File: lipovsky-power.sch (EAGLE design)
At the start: 95 parts, among them J1 M04-929J, J2 M04-929J, J3 M04-929J, J4 M04-929J, Q1 NMOS30V_30A, Q12 NMOS40V_10A, Q14 NMOS40V_10A, Q16 NMOS40V_10A, Q18 NMOS40V_10A, Q21 PMOS30V_11A, Q22 PMOS30V_11A, Q23 NMOS40V_10A, Q24 NMOS40V_10A, Q25 PMOS30V_11A, Q26 PMOS30V_11A, Q27 NMOS40V_10A, Q28 NMOS40V_10A, Q3 2PMOS50V_0.17A, Q31 PMOS30V_11A, Q32 PMOS30V_11A, Q33 PMOS30V_11A, Q34 PMOS30V_11A, Q35 PMOS30V_11A, Q36 PMOS30V_11A, Q37 PMOS30V_11A, Q38 PMOS30V_11A, Q4 2PMOS50V_0.17A, Q41 PMOS30V_11A, Q42 PMOS30V_11A, Q43 PMOS30V_11A, Q44 PMOS30V_11A, Q45 PMOS30V_11A, Q46 PMOS30V_11A, Q47 PMOS30V_11A, Q48 PMOS30V_11A, Q5 2NMOS30V_0.1A, Q51 PMOS30V_11A, Q52 PMOS30V_11A, Q53 PMOS30V_11A, Q54 PMOS30V_11A, Q55 PMOS30V_11A, Q56 PMOS30V_11A, Q57 PMOS30V_11A, Q58 PMOS30V_11A, Q62 PMOS30V_11A, Q64 PMOS30V_11A, Q66 PMOS30V_11A, Q68 PMOS30V_11A, T1 TFORM_4_4311_4A4, U1 DG508BEN-T1-GE4, U2 DG508BEN-T1-GE4, U4 LTC3805-5IDD, U6 AR30N60PPA-13

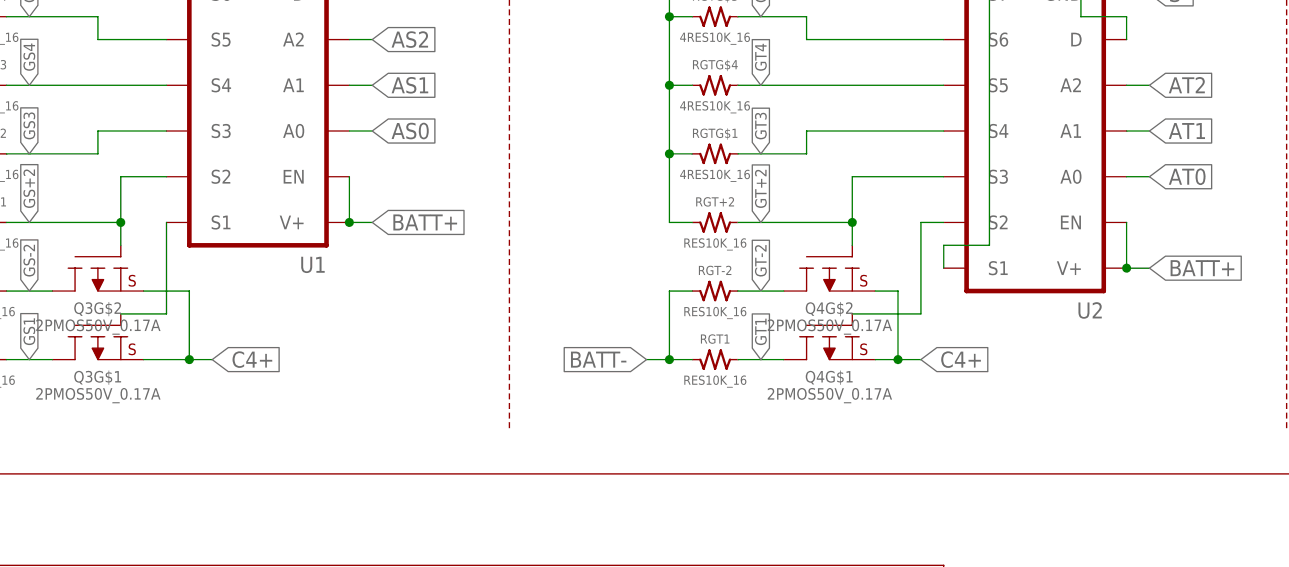
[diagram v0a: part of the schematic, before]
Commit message: Missed a couple pmos gate pull-ups
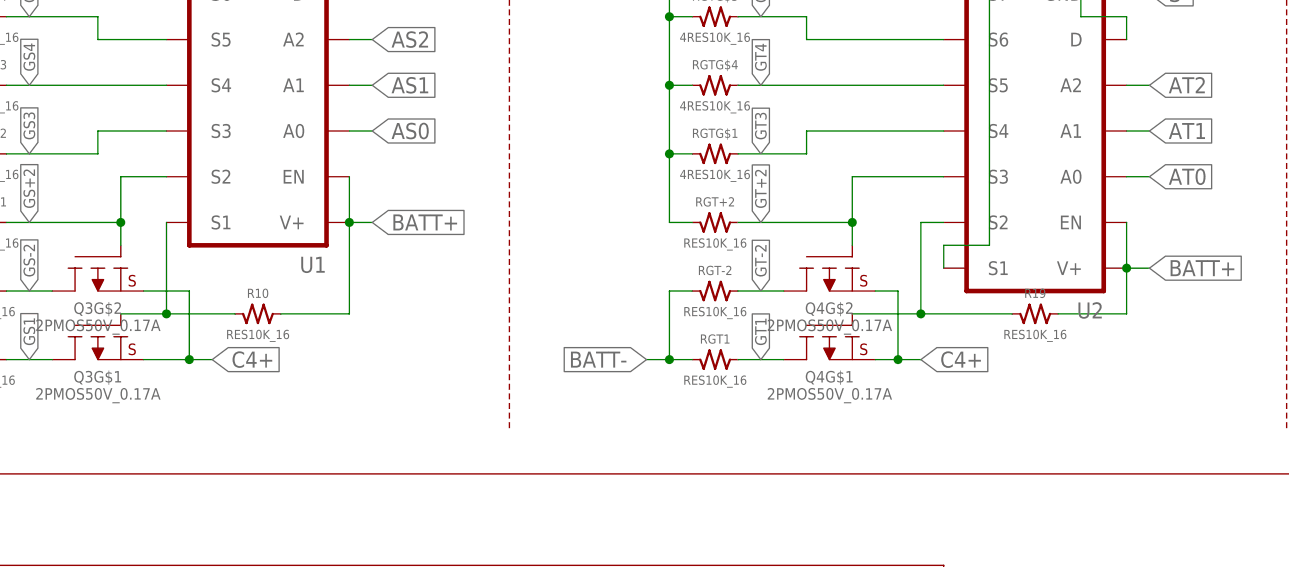
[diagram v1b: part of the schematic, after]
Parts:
- added R10, R19: RES10K_16, dubec:RES10K_16
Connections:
- net !GS1: now also R10.1
- net !GT1: now also R19.1
- net BATT+: now also R10.2, R19.2
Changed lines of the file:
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@@
 <part name="D1" library="dubec" deviceset="D_ZENER" device="18V_0.3W"/>
 <part name="R4" library="dubec" deviceset="RES" device="15.4K_16"/>
+<part name="R10" library="dubec" deviceset="RES" device="10K_16"/>
+<part name="R19" library="dubec" deviceset="RES" device="10K_16"/>
 </parts>
 <sheets>
@@
 <instance part="D1" gate="G$1" x="43.18" y="38.1" rot="R270"/>
 <instance part="R4" gate="G$1" x="27.94" y="38.1" rot="R90"/>
+<instance part="R10" gate="G$1" x="114.3" y="22.86"/>
+<instance part="R19" gate="G$1" x="200.66" y="22.86"/>
 </instances>
 <busses>
@@
 <wire x1="124.46" y1="38.1" x2="124.46" y2="33.02" width="0.1524" layer="91"/>
 <junction x="124.46" y="33.02"/>
+<wire x1="124.46" y1="33.02" x2="124.46" y2="22.86" width="0.1524" layer="91"/>
+<wire x1="124.46" y1="22.86" x2="116.84" y2="22.86" width="0.1524" layer="91"/>
+<pinref part="R10" gate="G$1" pin="2"/>
 </segment>
 <segment>
@@
 <wire x1="210.82" y1="33.02" x2="210.82" y2="27.94" width="0.1524" layer="91"/>
 <junction x="210.82" y="27.94"/>
+<pinref part="R19" gate="G$1" pin="2"/>
+<wire x1="203.2" y1="22.86" x2="210.82" y2="22.86" width="0.1524" layer="91"/>
+<wire x1="210.82" y1="22.86" x2="210.82" y2="27.94" width="0.1524" layer="91"/>
 </segment>
 </net>
@@
 <pinref part="U2" gate="G$1" pin="S2"/>
 <wire x1="190.5" y1="33.02" x2="187.96" y2="33.02" width="0.1524" layer="91"/>
+<pinref part="R19" gate="G$1" pin="1"/>
+<wire x1="187.96" y1="22.86" x2="198.12" y2="22.86" width="0.1524" layer="91"/>
+<junction x="187.96" y="22.86"/>
 </segment>
 </net>
@@
 <pinref part="Q3" gate="G$1" pin="G"/>
 <wire x1="104.14" y1="22.86" x2="99.06" y2="22.86" width="0.1524" layer="91"/>
-</segment>
-</net>
+<wire x1="104.14" y1="22.86" x2="111.76" y2="22.86" width="0.1524" layer="91"/>
+<junction x="104.14" y="22.86"/>
+<pinref part="R10" gate="G$1" pin="1"/>
+</segment>
+</net>

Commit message: test point
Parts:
- added TP4: TEST-POINT3, SparkFun-Passives:TEST-POINT3
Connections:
- net SS-5: now also TP4.1
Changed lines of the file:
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@@
 <part name="R10" library="dubec" deviceset="RES" device="10K_16"/>
 <part name="R19" library="dubec" deviceset="RES" device="10K_16"/>
+<part name="TP4" library="SparkFun-Passives" deviceset="TEST-POINT" device="3"/>
 </parts>
 <sheets>
@@
 <instance part="R10" gate="G$1" x="114.3" y="22.86"/>
 <instance part="R19" gate="G$1" x="200.66" y="22.86"/>
+<instance part="TP4" gate="G$1" x="-93.98" y="20.32" rot="R270"/>
 </instances>
 <busses>
@@
 <net name="SS+5" class="0">
 <segment>
-<wire x1="-96.52" y1="33.02" x2="-91.44" y2="33.02" width="0.1524" layer="91"/>
 <pinref part="Q51" gate="G$1" pin="S"/>
 <pinref part="Q52" gate="G$1" pin="S"/>
+<wire x1="-96.52" y1="33.02" x2="-91.44" y2="33.02" width="0.1524" layer="91"/>
 </segment>
 </net>
 <net name="SS-5" class="0">
 <segment>
-<wire x1="-91.44" y1="22.86" x2="-96.52" y2="22.86" width="0.1524" layer="91"/>
+<wire x1="-91.44" y1="22.86" x2="-93.98" y2="22.86" width="0.1524" layer="91"/>
 <pinref part="Q54" gate="G$1" pin="S"/>
 <pinref part="Q53" gate="G$1" pin="S"/>
-</segment>
-</net>
+<pinref part="TP4" gate="G$1" pin="1"/>
+<wire x1="-93.98" y1="22.86" x2="-96.52" y2="22.86" width="0.1524" layer="91"/>
+<wire x1="-93.98" y1="20.32" x2="-93.98" y2="22.86" width="0.1524" layer="91"/>
+<junction x="-93.98" y="22.86"/>
+</segment>
+</net>

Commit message: .
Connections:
- net FB: now also MVOE.PA7
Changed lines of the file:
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@@
 <wire x1="241.3" y1="-48.26" x2="241.3" y2="-45.72" width="0.1524" layer="91"/>
+</segment>
+<segment>
+<pinref part="MVOE" gate="G$1" pin="PA7"/>
+<wire x1="274.32" y1="48.26" x2="276.86" y2="48.26" width="0.1524" layer="91"/>
+<label x="276.86" y="48.26" size="1.27" layer="95" xref="yes"/>
 </segment>
 </net>

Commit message: 2S boost
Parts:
- removed D4: D_ZENER2.4V, dubec:D_ZENER2.4V
- removed MVOE: ATTINYX4A2MMHR, dubec:ATTINYX4A2MMHR
- added CB1, CB2, CB3: CAP4.7UF_10V, dubec:CAP4.7UF_10V
- added D2: D_ZENER2.4V, dubec:D_ZENER2.4V
- added DB1: 2D_SCHOTTKY40V_0.2A, dubec:2D_SCHOTTKY40V_0.2A
- added U3: DG508BEN-T1-GE4, dubec:DG508BEN-T1-GE4
- added U5: LM2665M6, dubec:LM2665M6
- U1: value DG508BEN-T1-GE4 -> LTC3805-5IDD; device dubec:DG508BEN-T1-GE4 -> dubec:LTC3805-5IDD
- U2: value DG508BEN-T1-GE4 -> ATTINYX4A2MMHR; device dubec:DG508BEN-T1-GE4 -> dubec:ATTINYX4A2MMHR
- U4: value LTC3805-5IDD -> DG508BEN-T1-GE4; device dubec:LTC3805-5IDD -> dubec:DG508BEN-T1-GE4
- renumbered U$2 to JP2, U$3 to DA1, U$4 to DA2
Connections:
- new net 2SBOOST: CB3.2, DB1G$1.A, DB1G$2.C, U5.OUT
- new net N$11: CB2.1, U5.CAP-
- new net N$2: CB1.2, DB1G$2.A, U5.V+
- new net N$9: CB2.2, U5.CAP+
- net !GS1: now also U3.S1; no longer U1.S1
- net !GT1: now also U4.S2; no longer U2.S2
- net !S_RESET: now also U2.PB3; no longer MVOE.PB3
- net +5V: now also U2.VCC; no longer MVOE.VCC
- net +8V: now also U1.VCC; no longer U4.VCC
- net AS0: now also U2.PA2, U3.A0; no longer MVOE.PA2, U1.A0
- net AS1: now also U2.PA1, U3.A1; no longer MVOE.PA1, U1.A1
- net AS2: now also U2.PA0, U3.A2; no longer MVOE.PA0, U1.A2
- net AT0: now also U2.PB2, U4.A0; no longer MVOE.PB2, U2.A0
- net AT1: now also U2.PB1, U4.A1; no longer MVOE.PB1, U2.A1
- net AT2: now also U2.PB0, U4.A2; no longer MVOE.PB0, U2.A2
- net BATT+: now also U3.EN, U3.V+, U4.EN, U4.V+; no longer U1.EN, U1.V+, U2.EN, U2.V+
- net BATT-: now also U3.D, U3.S7, U3.S8, U3.V-, U4.D, U4.S1, U4.S8, U4.V-; no longer U1.D, U1.S7, U1.S8, U1.V-, U2.D, U2.S1, U2.S8, U2.V-
- net C1: now also CB3.1, U5.GND, U5.SD
- net C2: now also CB1.1
- net C4+: now also DB1G$1.C
- net EN_FLYBACK: now also U1.RUN, U2.PA3; no longer MVOE.PA3, U4.RUN
- net FB: now also U2.PA7; no longer MVOE.PA7
- net GS+2: now also U3.S2; no longer U1.S2
- net GS3: now also U3.S3; no longer U1.S3
- net GS4: now also U3.S4; no longer U1.S4
- net GS5: now also U3.S5; no longer U1.S5
- net GS6: now also U3.S6; no longer U1.S6
- net GT+2: now also U4.S3; no longer U2.S3
- net GT3: now also U4.S4; no longer U2.S4
- net GT4: now also U4.S5; no longer U2.S5
- net GT5: now also U4.S6; no longer U2.S6
- net GT6: now also U4.S7; no longer U2.S7
- net MISO: now also U2.PA5; no longer MVOE.PA5
- net N$1: now also D2.C, U1.FB; no longer D4.C, U4.FB
- net N$12: now also U1.I_TH; no longer U4.I_TH
- net N$3: now also U1.FS; no longer U4.FS
- net N$4: now also U1.OC; no longer U4.OC
- net N$5: now also U1.GATE; no longer U4.GATE
- net N$6: now also U1.I_SENSE; no longer U4.I_SENSE
- net S-: now also D2.A, U1.SYNC, U3.GND; no longer D4.A, MVOE.GND, U4.SYNC
- net SCL: now also U2.PA4; no longer MVOE.PA4
- net SDA: now also U2.PA6; no longer MVOE.PA6
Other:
- note added: "2S Booster"
- moved on the sheet: J1, J2, J3, J4, JP1, Q12, Q14, Q16, Q18, Q21, Q22, Q23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

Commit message: Inductor routing
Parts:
- removed C9: CAP22P_50V, dubec:CAP22P_50V
- removed JP2: JUMPER-PAD, dubec:JUMPER-PAD
- removed Q5: 2NMOS30V_0.1A, dubec:2NMOS30V_0.1A
- removed R11: RES10K_16, dubec:RES10K_16
- removed R12: RES590_16, dubec:RES590_16
- removed R13: RES2.2K_16, dubec:RES2.2K_16
- removed R14: RES5.1K_16, dubec:RES5.1K_16
- removed R15: RES100K_16, dubec:RES100K_16
- removed T1: TFORM_4_4311_4A4, dubec:TFORM_4_4311_4A4
- removed TP2: TEST-POINT3, SparkFun-Passives:TEST-POINT3
- removed U6: AR30N60PPA-13, dubec:AR30N60PPA-13
- added L1: COUPINDSRF1260A3R3Y, dubec:COUPINDSRF1260A3R3Y
- C5: value CAP220U_6V3 -> CAP100UF_10V; device dubec:CAP220U_6V3 -> dubec:CAP100UF_10V
- D2: value D_ZENER2.4V -> D_SCH30V_5A; device dubec:D_ZENER2.4V -> dubec:D_SCH30V_5A
- R6: value RES61.9K_16 -> RES36K_16; device dubec:RES61.9K_16 -> dubec:RES36K_16
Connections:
- removed net N$1: D2.C, R11.1, U1.FB
- removed net N$18: C9.1, Q5G$1.D, R12.2
- removed net N$20: C9.2, R13.1
- removed net N$21: R13.2, U6.SYNC
- removed net N$24: R14.2, U6.TON
- removed net N$25: R15.2, U6.TOFF/EN
- removed net N$26: T1.1, U6.VD
- removed net N$8: T1.4, TP2.1
- removed net SFB: Q5G$2.G, U6.SFB
- net +8V: no longer R12.1
- net FB: no longer R11.2
- net N$10: now also L1.A2; no longer T1.5, T1.7
- net N$5: no longer Q5G$1.G
- net N$7: now also D2.A, L1.B2; no longer JP2.2, T1.3
- net OPTO_C: no longer Q5G$2.D
- net S+: now also L1.A1; no longer T1.6, T1.8
- net S-: now also U1.FB; no longer D2.A, Q5G$1.S
- net T+: now also D2.C; no longer T1.2, U6.VCC
- net T-: now also L1.B1; no longer JP2.1, Q5G$2.S, R14.1, R15.1, U6.GND, U6.VS
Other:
- moved on the sheet: C10, C5, R9

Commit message: "finished"
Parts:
- removed C4: CAP47N_25V, dubec:CAP47N_25V
- added D3: D_SCH30V_0.2A, dubec:D_SCH30V_0.2A
- R7: value RES2.2K_16 -> RES18.2K_16; device dubec:RES2.2K_16 -> dubec:RES18.2K_16
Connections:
- removed net N$12: R7.2, U1.I_TH
- removed net N$17: C4.2, R7.1
- new net N$1: D3.A, U1.I_TH
- new net TH: D3.C, R7.1
- net +8V: now also R7.2
- net S-: no longer C4.1
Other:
- moved on the sheet: C10, CB1, CB2, CB3, D2, DB1G$2, J1, J2, J3, J4, JP1, L1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

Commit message: Power board finished now
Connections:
- removed net TH: D3.C, R7.1
- net !S_RESET: now also J3.1; no longer J3.4
- net FB: now also D3.C, R7.1
- net SCL: now also J3.4; no longer J3.1
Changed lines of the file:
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@@
 <label x="276.86" y="48.26" size="1.27" layer="95" xref="yes"/>
+</segment>
+<segment>
+<pinref part="D3" gate="G$1" pin="C"/>
+<wire x1="33.02" y1="-66.04" x2="30.48" y2="-66.04" width="0.1524" layer="91"/>
+<label x="30.48" y="-66.04" size="1.778" layer="95" rot="R180" xref="yes"/>
+</segment>
+<segment>
+<wire x1="93.98" y1="-58.42" x2="88.9" y2="-58.42" width="0.1524" layer="91"/>
+<wire x1="88.9" y1="-58.42" x2="88.9" y2="-50.8" width="0.1524" layer="91"/>
+<label x="88.9" y="-55.88" size="1.778" layer="95" rot="R180" xref="yes"/>
+<pinref part="R7" gate="G$1" pin="1"/>
 </segment>
 </net>
@@
 </segment>
 <segment>
-<pinref part="J3" gate="G$1" pin="4"/>
-<wire x1="-25.4" y1="-73.66" x2="-25.4" y2="-71.12" width="0.1524" layer="91"/>
-<label x="-25.4" y="-71.12" size="1.27" layer="95" rot="R90" xref="yes"/>
+<label x="-17.78" y="-71.12" size="1.27" layer="95" rot="R90" xref="yes"/>
+<pinref part="J3" gate="G$1" pin="1"/>
+<wire x1="-17.78" y1="-71.12" x2="-17.78" y2="-73.66" width="0.1524" layer="91"/>
 </segment>
 </net>
 <net name="SCL" class="0">
 <segment>
-<label x="-17.78" y="-71.12" size="1.27" layer="95" rot="R90" xref="yes"/>
-<pinref part="J3" gate="G$1" pin="1"/>
-<wire x1="-17.78" y1="-71.12" x2="-17.78" y2="-73.66" width="0.1524" layer="91"/>
+<label x="-25.4" y="-71.12" size="1.27" layer="95" rot="R90" xref="yes"/>
+<pinref part="J3" gate="G$1" pin="4"/>
+<wire x1="-25.4" y1="-71.12" x2="-25.4" y2="-73.66" width="0.1524" layer="91"/>
 </segment>
 <segment>
@@
 </segment>
 </net>
-<net name="TH" class="0">
-<segment>
-<pinref part="D3" gate="G$1" pin="C"/>
-<wire x1="33.02" y1="-66.04" x2="30.48" y2="-66.04" width="0.1524" layer="91"/>
-<label x="30.48" y="-66.04" size="1.778" layer="95" rot="R180" xref="yes"/>
-</segment>
-<segment>
-<wire x1="93.98" y1="-58.42" x2="88.9" y2="-58.42" width="0.1524" layer="91"/>
-<wire x1="88.9" y1="-58.42" x2="88.9" y2="-50.8" width="0.1524" layer="91"/>
-<label x="88.9" y="-55.88" size="1.778" layer="95" rot="R180" xref="yes"/>
-<pinref part="R7" gate="G$1" pin="1"/>
-</segment>
-</net>

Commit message: Compaction finished
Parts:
- removed R17: RES330_16, dubec:RES330_16
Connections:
- removed net OPTO_A: J2.2, R17.1
- net OPTO_C: now also J2.2; no longer J2.1
- net T+: now also J2.1; no longer R17.2
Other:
- moved on the sheet: D2
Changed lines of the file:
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@@
 <part name="C8" library="dubec" deviceset="CAP" device="4.7U_10V" value="CAP4.7U_10V"/>
 <part name="C10" library="dubec" deviceset="CAP" device="47UF_10V"/>
-<part name="R17" library="dubec" deviceset="RES" device="330_16" value="RES330_16"/>
 <part name="R18" library="dubec" deviceset="RES" device="1K_16" value="RES1K_16"/>
 <part name="J2" library="dubec" deviceset="M04" device="-929J"/>
@@
 <instance part="C8" gate="G$1" x="259.08" y="58.42"/>
 <instance part="C10" gate="G$1" x="124.46" y="-38.1" rot="R90"/>
-<instance part="R17" gate="G$1" x="109.22" y="-53.34" rot="R90"/>
 <instance part="R18" gate="G$1" x="109.22" y="-63.5" rot="R180"/>
 <instance part="Q3" gate="G$2" x="96.52" y="25.4" rot="MR270"/>
@@
 <instance part="L1" gate="G$1" x="99.06" y="-30.48"/>
 <instance part="R6" gate="G$1" x="35.56" y="-60.96"/>
-<instance part="D2" gate="G$1" x="111.76" y="-33.02"/>
+<instance part="D2" gate="G$1" x="109.22" y="-33.02"/>
 <instance part="D3" gate="G$1" x="35.56" y="-66.04" rot="R180"/>
 <instance part="R7" gate="G$1" x="88.9" y="-48.26" rot="R90"/>
@@
 <pinref part="C10" gate="G$1" pin="1"/>
 <pinref part="R18" gate="G$1" pin="1"/>
-<wire x1="111.76" y1="-63.5" x2="116.84" y2="-63.5" width="0.1524" layer="91"/>
+<wire x1="111.76" y1="-63.5" x2="114.3" y2="-63.5" width="0.1524" layer="91"/>
 <junction x="124.46" y="-63.5"/>
 <pinref part="L1" gate="G$1" pin="B1"/>
-<wire x1="116.84" y1="-63.5" x2="124.46" y2="-63.5" width="0.1524" layer="91"/>
-<wire x1="104.14" y1="-27.94" x2="116.84" y2="-27.94" width="0.1524" layer="91"/>
-<wire x1="116.84" y1="-27.94" x2="116.84" y2="-63.5" width="0.1524" layer="91"/>
-<junction x="116.84" y="-63.5"/>
+<wire x1="114.3" y1="-63.5" x2="124.46" y2="-63.5" width="0.1524" layer="91"/>
+<wire x1="104.14" y1="-27.94" x2="114.3" y2="-27.94" width="0.1524" layer="91"/>
+<wire x1="114.3" y1="-27.94" x2="114.3" y2="-63.5" width="0.1524" layer="91"/>
+<junction x="114.3" y="-63.5"/>
 </segment>
 <segment>
@@
 <wire x1="124.46" y1="-33.02" x2="124.46" y2="-35.56" width="0.1524" layer="91"/>
 <junction x="124.46" y="-33.02"/>
-<pinref part="R17" gate="G$1" pin="2"/>
-<wire x1="109.22" y1="-43.18" x2="109.22" y2="-50.8" width="0.1524" layer="91"/>
-<wire x1="109.22" y1="-43.18" x2="119.38" y2="-43.18" width="0.1524" layer="91"/>
-<wire x1="119.38" y1="-43.18" x2="119.38" y2="-33.02" width="0.1524" layer="91"/>
+<wire x1="109.22" y1="-48.26" x2="119.38" y2="-48.26" width="0.1524" layer="91"/>
+<wire x1="119.38" y1="-48.26" x2="119.38" y2="-33.02" width="0.1524" layer="91"/>
 <pinref part="D2" gate="G$1" pin="C"/>
-<wire x1="114.3" y1="-33.02" x2="119.38" y2="-33.02" width="0.1524" layer="91"/>
+<wire x1="111.76" y1="-33.02" x2="119.38" y2="-33.02" width="0.1524" layer="91"/>
 <junction x="119.38" y="-33.02"/>
+<wire x1="109.22" y1="-48.26" x2="109.22" y2="-58.42" width="0.1524" layer="91"/>
+<wire x1="109.22" y1="-58.42" x2="104.14" y2="-58.42" width="0.1524" layer="91"/>
 </segment>
 <segment>
@@
 <wire x1="-38.1" y1="-96.52" x2="-38.1" y2="-99.06" width="0.1524" layer="91"/>
 <label x="-38.1" y="-99.06" size="1.27" layer="95" rot="R270" xref="yes"/>
+</segment>
+<segment>
+<pinref part="J2" gate="G$1" pin="1"/>
+<wire x1="-25.4" y1="-96.52" x2="-25.4" y2="-99.06" width="0.1524" layer="91"/>
+<label x="-25.4" y="-99.06" size="1.27" layer="95" rot="R270" xref="yes"/>
 </segment>
 </net>
@@
 <segment>
 <pinref part="D3" gate="G$1" pin="C"/>
-<wire x1="33.02" y1="-66.04" x2="30.48" y2="-66.04" width="0.1524" layer="91"/>
-<label x="30.48" y="-66.04" size="1.778" layer="95" rot="R180" xref="yes"/>
+<wire x1="33.02" y1="-66.04" x2="20.32" y2="-66.04" width="0.1524" layer="91"/>
+<label x="20.32" y="-66.04" size="1.778" layer="95" rot="R180" xref="yes"/>
 </segment>
 <segment>
 <wire x1="93.98" y1="-58.42" x2="88.9" y2="-58.42" width="0.1524" layer="91"/>
 <wire x1="88.9" y1="-58.42" x2="88.9" y2="-50.8" width="0.1524" layer="91"/>
-<label x="88.9" y="-55.88" size="1.778" layer="95" rot="R180" xref="yes"/>
+<label x="88.9" y="-58.42" size="1.778" layer="95" rot="R180" xref="yes"/>
 <pinref part="R7" gate="G$1" pin="1"/>
 </segment>
 </net>
-<net name="OPTO_A" class="0">
-<segment>
-<pinref part="R17" gate="G$1" pin="1"/>
-<wire x1="109.22" y1="-55.88" x2="109.22" y2="-58.42" width="0.1524" layer="91"/>
-<wire x1="109.22" y1="-58.42" x2="104.14" y2="-58.42" width="0.1524" layer="91"/>
-<label x="104.14" y="-58.42" size="1.778" layer="95" rot="R90" xref="yes"/>
+<net name="OPTO_C" class="0">
+<segment>
+<pinref part="R18" gate="G$1" pin="2"/>
+<wire x1="104.14" y1="-63.5" x2="106.68" y2="-63.5" width="0.1524" layer="91"/>
+<label x="104.14" y="-63.5" size="1.778" layer="95" rot="R270" xref="yes"/>
 </segment>
 <segment>
@@
 <pinref part="J2" gate="G$1" pin="2"/>
 <wire x1="-22.86" y1="-99.06" x2="-22.86" y2="-96.52" width="0.1524" layer="91"/>
-</segment>
-</net>
-<net name="OPTO_C" class="0">
-<segment>
-<pinref part="R18" gate="G$1" pin="2"/>
-<wire x1="104.14" y1="-63.5" x2="106.68" y2="-63.5" width="0.1524" layer="91"/>
-<label x="104.14" y="-63.5" size="1.778" layer="95" rot="R270" xref="yes"/>
-</segment>
-<segment>
-<label x="-25.4" y="-99.06" size="1.27" layer="95" rot="R270" xref="yes"/>
-<pinref part="J2" gate="G$1" pin="1"/>
-<wire x1="-25.4" y1="-99.06" x2="-25.4" y2="-96.52" width="0.1524" layer="91"/>
 </segment>
 </net>
@@
 <pinref part="L1" gate="G$1" pin="B2"/>
 <pinref part="D2" gate="G$1" pin="A"/>
-<wire x1="104.14" y1="-33.02" x2="109.22" y2="-33.02" width="0.1524" layer="91"/>
-</segment>
-</net>
+<wire x1="104.14" y1="-33.02" x2="106.68" y2="-33.02" width="0.1524" layer="91"/>
+</segment>
+</net>
